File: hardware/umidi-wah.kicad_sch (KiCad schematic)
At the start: 30 parts

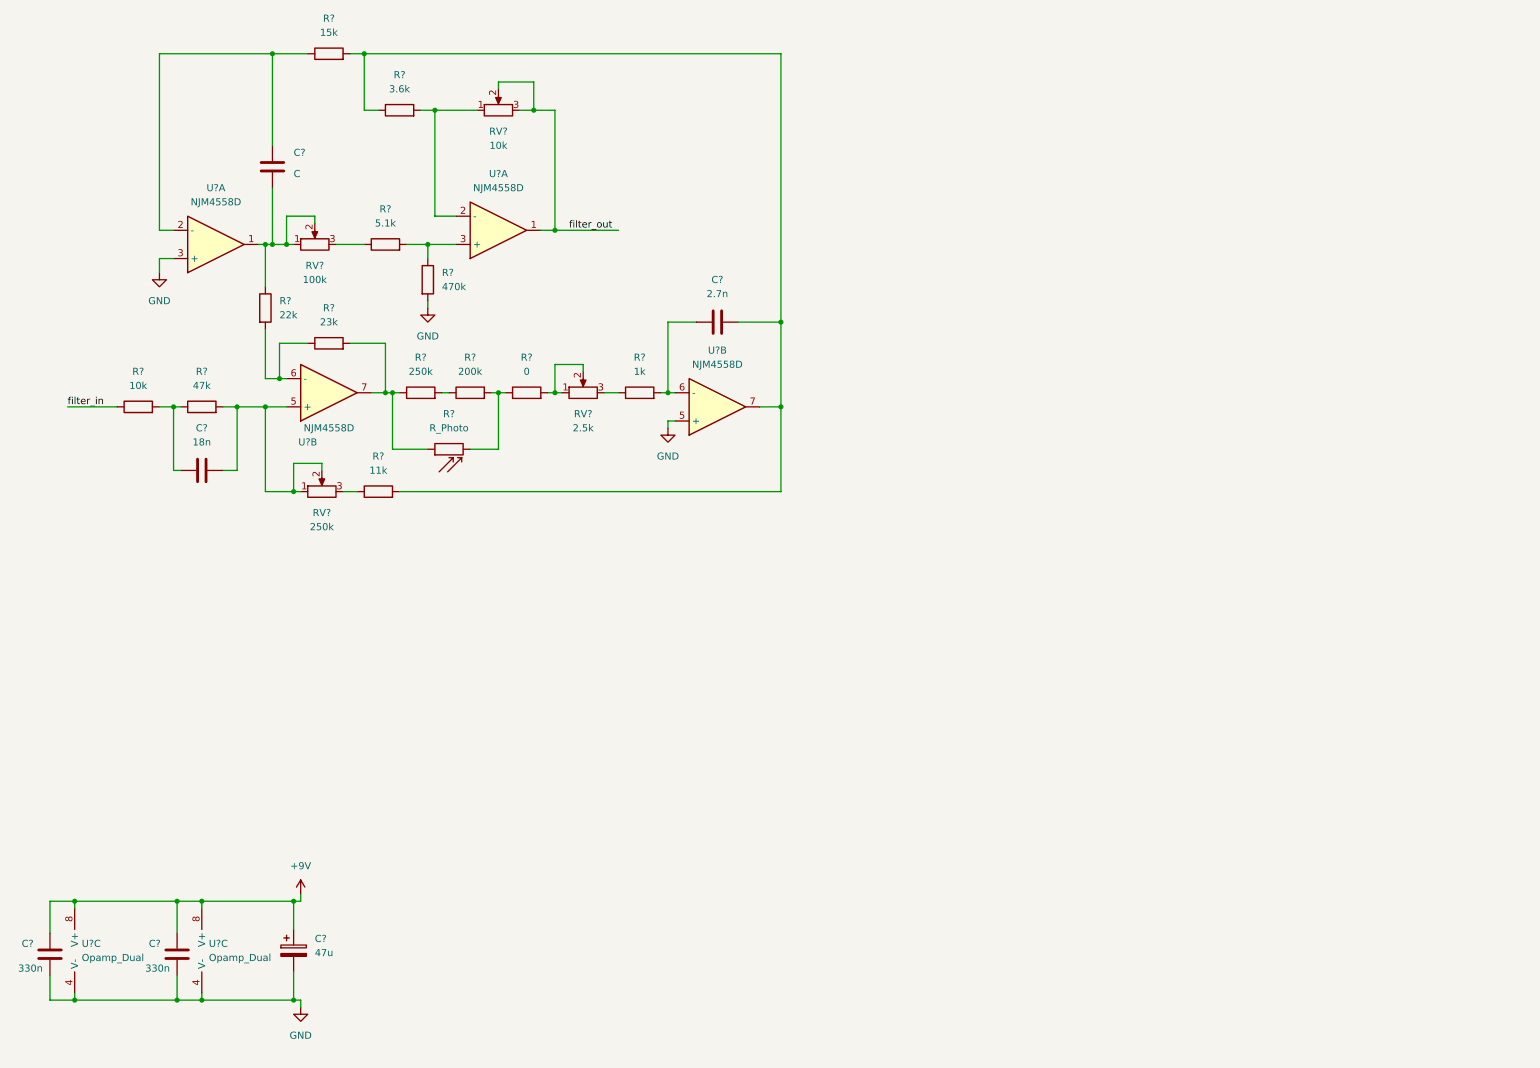
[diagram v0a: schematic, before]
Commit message: Add in/out buffers, loosely based on demon circuit
Keeping in mind that we will use a relay true bypass. Thus, we omitted the jfets and some dc blocks.
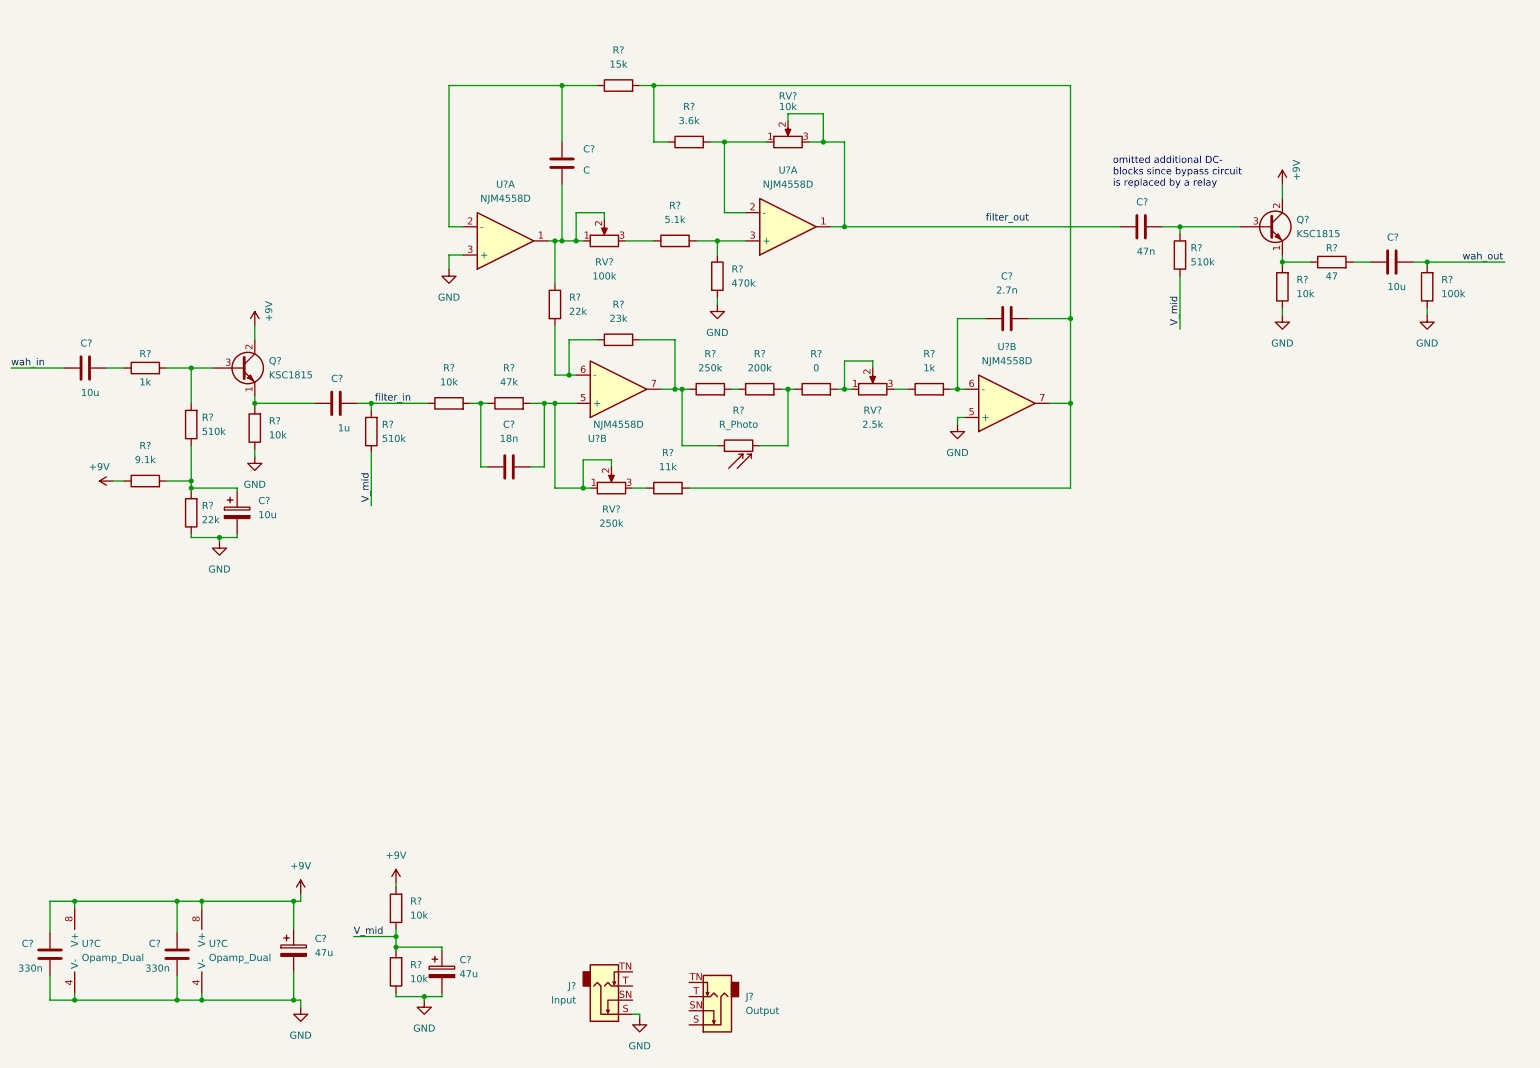
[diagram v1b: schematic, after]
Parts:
- added C?: 47n, symbol Device:C
- added C?: 10u, symbol Device:C_Polarized
- added C? (x2): 10u, symbol Device:C
- added C?: 47u, symbol Device:C_Polarized
- added C?: 1u, symbol Device:C
- added J?: Output, symbol Connector:AudioJack2_Switch
- added J?: Input, symbol Connector:AudioJack2_Switch
- added Q? (x2): KSC1815, Package_TO_SOT_THT:TO-92, symbol Device:Q_NPN_ECB
- added R? (x4): 10k, symbol Device:R
- added R?: 22k, symbol Device:R
- added R?: 100k, symbol Device:R
- added R?: 9.1k, symbol Device:R
- added R? (x3): 510k, symbol Device:R
- added R?: 1k, symbol Device:R
- added R?: 47, symbol Device:R
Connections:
- net +9V: now also Q?.2 (C), Q?.2 (C), R?.1, R?.2
- net GND: now also C?.2, C?.2, J?.S, R?.1, R?.1, R?.1, R?.1, R?.1
- net filter_in: now also C?.2, R?.2
- net filter_out: no longer RV?.2, RV?.3, U?.1
- new net: C?.1, R?.1, R?.2, R?.2
- new net: C?.1, RV?.2, RV?.3, U?.1
- new net: C?.1, Q?.1 (E), R?.2
- new net: C?.2, Q?.3 (B), R?.2
- new net: Q?.1 (E), R?.1, R?.2
- new net: Q?.3 (B), R?.2, R?.2
- new net: C?.1, R?.2
- new net: C?.2, R?.1
- new net V_mid: C?.1, R?.1, R?.1, R?.1, R?.2
- new net wah_in: C?.1
- new net wah_out: C?.2, R?.2
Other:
- note added: "omitted additional DC- blocks since bypass circuit is replaced by a relay"
- moved on the sheet: C?, R?, RV?, U?A, U?B

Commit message: Add bypass circuit
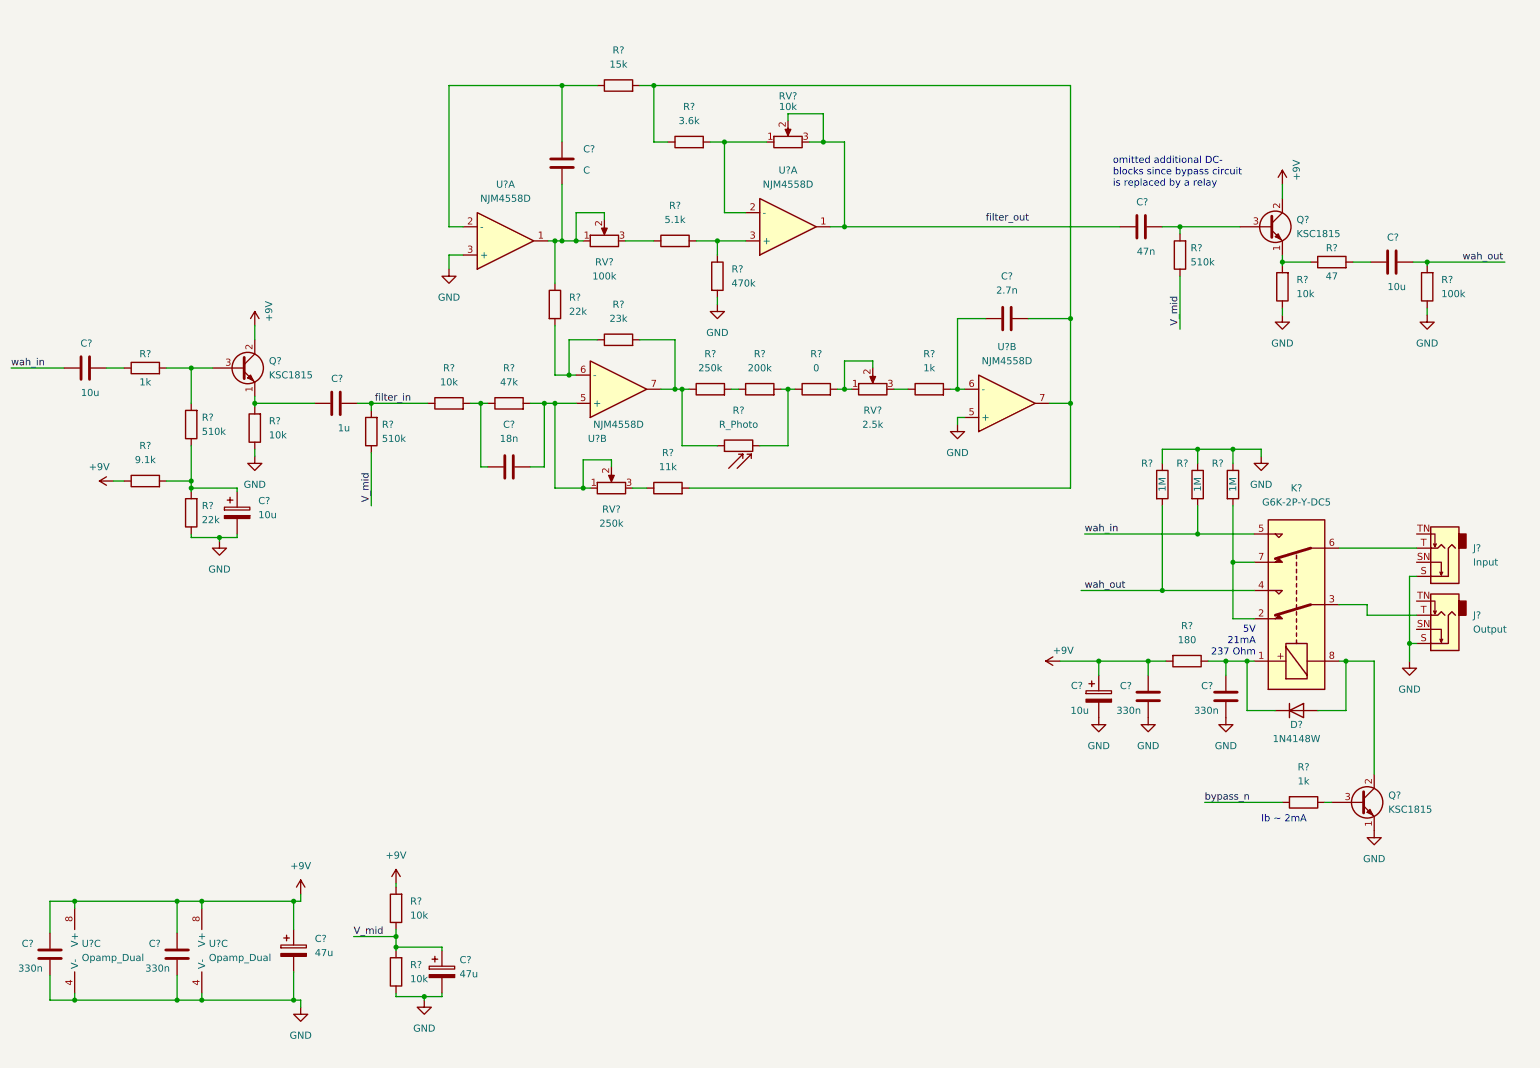
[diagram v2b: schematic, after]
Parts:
- added C? (x2): 330n, symbol Device:C
- added C?: 10u, symbol Device:C_Polarized
- added D?: 1N4148W, Diode_SMD:D_SOD-123, symbol Diode:1N4148W
- added K?: G6K-2P-Y-DC5, symbol Relay:G6K-2
- added Q?: KSC1815, Package_TO_SOT_THT:TO-92, symbol Device:Q_NPN_ECB
- added R? (x3): 1M, symbol Device:R
- added R?: 1k, symbol Device:R
- added R?: 180, symbol Device:R
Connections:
- net +9V: now also C?.1, C?.1, R?.2
- net GND: now also J?.S, C?.2, C?.2, C?.2, Q?.1 (E), R?.1, R?.1, R?.1
- net wah_in: now also K?.5, R?.2
- net wah_out: now also K?.4, R?.2
- net at J?.T: now also K?.3
- net at J?.T: now also K?.6
- new net: K?.2, K?.7, R?.2
- new net: C?.1, D?.1 (K), K?.1, R?.1
- new net: Q?.3 (B), R?.1
- new net: D?.2 (A), K?.8, Q?.2 (C)
- new net bypass_n: R?.2
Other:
- note added: "5V 21mA 237 Ohm"
- note added: "Ib ~ 2mA"
- moved on the sheet: J?

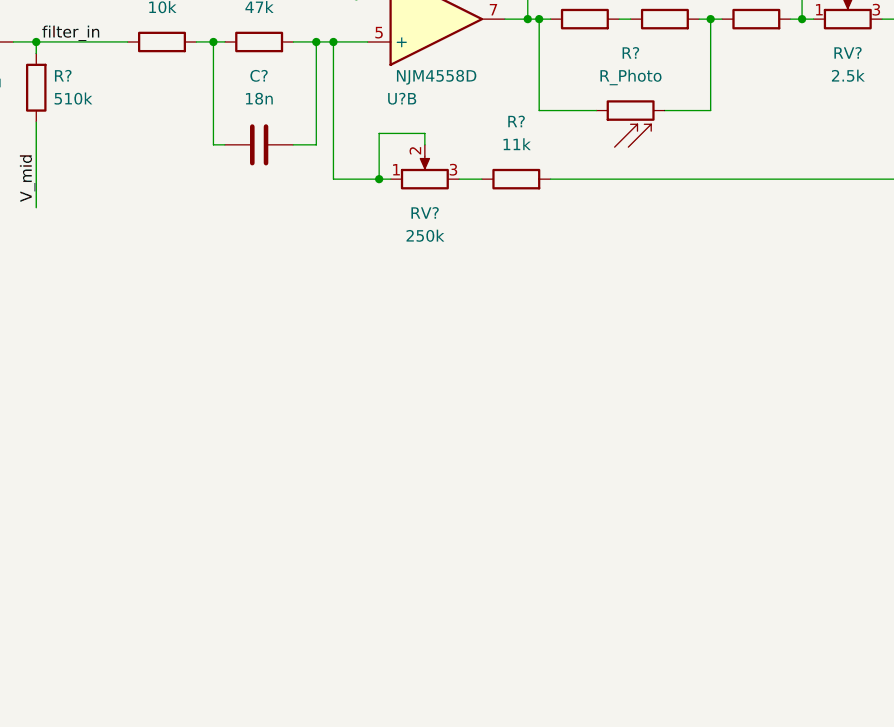
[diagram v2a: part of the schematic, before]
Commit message: Add led and filter circuit
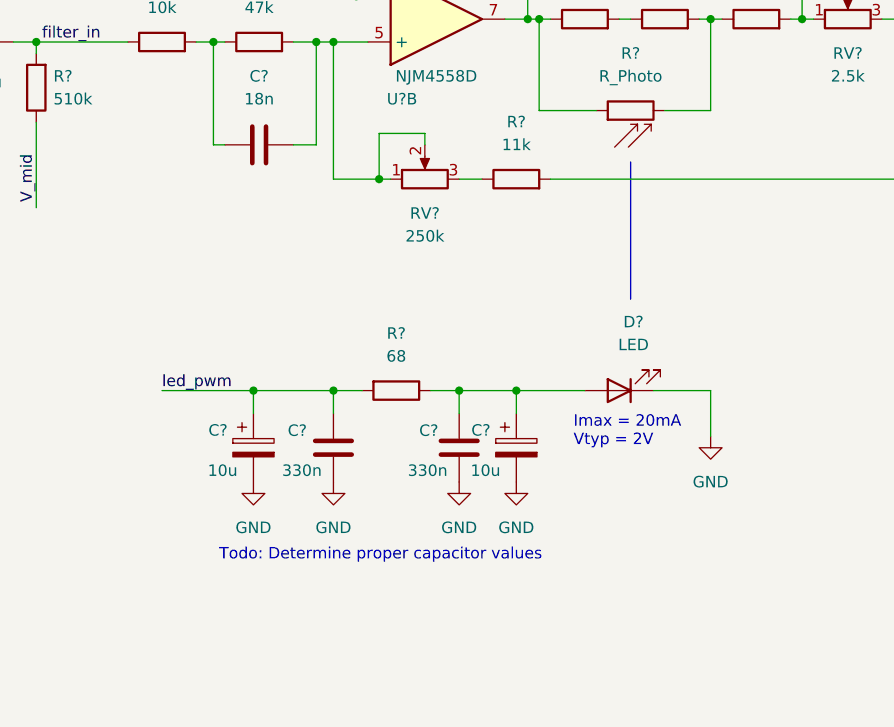
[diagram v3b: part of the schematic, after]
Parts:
- added C? (x2): 10u, symbol Device:C_Polarized
- added C? (x2): 330n, symbol Device:C
- added D?: LED, symbol Device:LED
- added R?: 68, symbol Device:R
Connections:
- net GND: now also C?.2, C?.2, C?.2, C?.2, D?.1 (K)
- new net: C?.1, C?.1, D?.2 (A), R?.1
- new net led_pwm: C?.1, C?.1, R?.2
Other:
- note added: "Imax = 20mA Vtyp = 2V"
- note added: "Todo: Determine proper capacitor values"

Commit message: Sketch umidi connection
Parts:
- added J?: Conn_02x05_Odd_Even, Connector_IDC:IDC-Header_2x05_P2.54mm_Vertical, symbol Connector_Generic:Conn_02x05_Odd_Even
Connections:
- net GND: now also J?.10 (Pin_10)
- new net umidi_3v3: J?.1 (Pin_1)
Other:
- note added: "Since the OP has a high input impedance: Is this input stage required?"
- note added: "uMidi GPIO1"
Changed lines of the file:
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@@
+    (stroke (width 0) (type default) (color 0 0 0 0))
+  )
+  (wire (pts (xy 134.62 184.15) (xy 148.59 184.15))
     (stroke (width 0) (type default) (color 0 0 0 0))
   )
@@
     (stroke (width 0) (type default) (color 0 0 0 0))
   )
+  (wire (pts (xy 165.1 187.96) (xy 166.37 187.96))
+    (stroke (width 0) (type default) (color 0 0 0 0))
+  )
   (wire (pts (xy 81.915 178.435) (xy 90.17 178.435))
     (stroke (width 0) (type default) (color 0 0 0 0))
@@
     (stroke (width 0) (type default) (color 0 0 0 0))
   )
+  (wire (pts (xy 137.16 189.23) (xy 147.32 189.23))
+    (stroke (width 0) (type default) (color 0 0 0 0))
+  )
   (wire (pts (xy 264.16 111.76) (xy 264.16 123.825))
     (stroke (width 0) (type default) (color 0 0 0 0))
@@
     (stroke (width 0) (type default) (color 0 0 0 0))
   )
+  (wire (pts (xy 139.7 177.8) (xy 152.4 177.8))
+    (stroke (width 0) (type default) (color 0 0 0 0))
+  )
   (wire (pts (xy 74.93 80.645) (xy 77.47 80.645))
     (stroke (width 0) (type default) (color 0 0 0 0))
@@
   )
   (wire (pts (xy 46.99 187.96) (xy 63.5 187.96))
+    (stroke (width 0) (type default) (color 0 0 0 0))
+  )
+  (wire (pts (xy 166.37 187.96) (xy 166.37 189.23))
     (stroke (width 0) (type default) (color 0 0 0 0))
   )
@@
     (effects (font (size 1.27 1.27)) (justify left bottom))
   )
+  (text "Since the OP has a high input impedance:\nIs this input stage required?"
+    (at 40.64 60.96 0)
+    (effects (font (size 1.27 1.27)) (justify left bottom))
+  )
   (text "Ib ~ 2mA" (at 237.49 156.21 0)
     (effects (font (size 1.27 1.27)) (justify left bottom))
   )
+  (text "uMidi GPIO1" (at 152.4 193.04 0)
+    (effects (font (size 1.27 1.27)) (justify left bottom))
+  )
   (text "5V\n21mA\n237 Ohm" (at 236.5174 126.2127 180)
     (effects (font (size 1.27 1.27)) (justify right bottom))
@@
     (effects (font (size 1.27 1.27)) (justify left bottom))
   )
+  (label "umidi_3v3" (at 139.7 177.8 0)
+    (effects (font (size 1.27 1.27)) (justify left bottom))
+  )
+  (label "led_pwm" (at 137.16 189.23 0)
+    (effects (font (size 1.27 1.27)) (justify left bottom))
+  )
   (label "filter_out" (at 187.96 48.26 0)
+    (effects (font (size 1.27 1.27)) (justify left bottom))
+  )
+  (label "bypass_n" (at 134.62 184.15 0)
     (effects (font (size 1.27 1.27)) (justify left bottom))
   )
@@
     (pin "2")
   )
+  (symbol (lib_id "Connector_Generic:Conn_02x05_Odd_Even") (at 157.48 182.88 0) (unit 1)
+    (in_bom yes) (on_board yes) (fields_autoplaced)
+    (property "Reference" "J?" (id 0) (at 158.75 171.45 0))
+    (property "Value" "Conn_02x05_Odd_Even" (id 1) (at 158.75 173.99 0))
+    (property "Footprint" "Connector_IDC:IDC-Header_2x05_P2.54mm_Vertical" (id 2) (at 157.48 182.88 0)
+      (effects (font (size 1.27 1.27)) hide)
+    )
+    (property "Datasheet" "~" (id 3) (at 157.48 182.88 0)
+      (effects (font (size 1.27 1.27)) hide)
+    )
+    (pin "1")
+    (pin "10")
+    (pin "2")
+    (pin "3")
+    (pin "4")
+    (pin "5")
+    (pin "6")
+    (pin "7")
+    (pin "8")
+    (pin "9")
+  )
   (symbol (lib_id "Device:Q_NPN_ECB") (at 53.975 74.295 0) (unit 1)
     (in_bom yes) (on_board yes) (fields_autoplaced)
@@
     (pin "2")
   )
+  (symbol (lib_id "power:GND") (at 166.37 189.23 0) (unit 1)
+    (in_bom yes) (on_board yes) (fields_autoplaced)
+    (property "Reference" "#PWR?" (id 0) (at 166.37 195.58 0)
+      (effects (font (size 1.27 1.27)) hide)
+    )
+    (property "Value" "GND" (id 1) (at 166.37 194.31 0))
+    (property "Footprint" "" (id 2) (at 166.37 189.23 0)
+      (effects (font (size 1.27 1.27)) hide)
+    )
+    (property "Datasheet" "" (id 3) (at 166.37 189.23 0)
+      (effects (font (size 1.27 1.27)) hide)
+    )
+    (pin "1")
+  )
   (symbol (lib_id "Device:R") (at 110.49 62.865 0) (unit 1)
     (in_bom yes) (on_board yes) (fields_autoplaced)
@@
       (reference "#PWR?") (unit 1) (value "GND") (footprint "")
     )
+    (path "/de542319-36c7-417d-9f4d-e194f4e24e4a"
+      (reference "#PWR?") (unit 1) (value "GND") (footprint "")
+    )
     (path "/e4cc47ec-0fdd-4315-9f98-e04a8e2bc21c"
       (reference "#PWR?") (unit 1) (value "+9V") (footprint "")
@@
       (reference "J?") (unit 1) (value "Input") (footprint "")
     )
+    (path "/a66d7ae6-cd12-4982-9c0a-f404e2ffbc4d"
+      (reference "J?") (unit 1) (value "Conn_02x05_Odd_Even") (footprint "Connector_IDC:IDC-Header_2x05_P2.54mm_Vertical")
+    )
     (path "/946873e3-913b-4a54-adcd-b367620e707d"
